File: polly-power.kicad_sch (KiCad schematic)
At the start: 53 parts, among them J1 Conn_02x04_Odd_Even, J2 Conn_02x05_Odd_Even, P1 Power, P2 Analog, P3 Digital, P4 Digital, P5 CONN_01X01, P6 CONN_01X01, P7 CONN_01X01, P8 CONN_01X01, P9 Arduino, Q1 BC547C, Q2 BC547C, U1 74LS04, U2 TL072, U3 74HC4051, U4 LM7805_TO220, U5 LM337_TO220, U6 MCP4922-EP, U7 MCP1541-TO, U8 LM4040LP-4.1

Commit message: Tidy up after migration
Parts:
- C10, C11, C4, C6, C9: symbol Device:CP1_Small -> Device:C_Polarized_Small
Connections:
- net -6.5V: now also C6.2; no longer C6.1
- net GNDA: now also C6.1; no longer C6.2
- no-connect marks 17 -> 18
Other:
- note added: "Voice param DAC multiplexer (pin 10/9/8): 1: CUTOFF 2: RESONANCE 3: MIXER 4: VCA 5: PWM 6: VCO_CV 7: WAVE_SEL 8: MOD_AMT"
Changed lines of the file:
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@@
   (junction (at 236.22 55.88) (diameter 0) (color 0 0 0 0)
   )
+  (junction (at 214.63 129.54) (diameter 0) (color 0 0 0 0)
+  )
   (junction (at 77.47 60.96) (diameter 0) (color 0 0 0 0)
   )
@@
   )
   (no_connect (at 125.73 121.92))
+  (no_connect (at 186.69 157.48))
   (no_connect (at 259.08 50.8))
   (no_connect (at 259.08 53.34))
@@
     (stroke (width 0) (type default) (color 0 0 0 0))
   )
+  (wire (pts (xy 215.9 127) (xy 214.63 127))
+    (stroke (width 0) (type default) (color 0 0 0 0))
+  )
   (wire (pts (xy 92.71 63.5) (xy 91.44 63.5))
     (stroke (width 0) (type default) (color 0 0 0 0))
@@
     (stroke (width 0) (type default) (color 0 0 0 0))
   )
+  (wire (pts (xy 214.63 127) (xy 214.63 129.54))
+    (stroke (width 0) (type default) (color 0 0 0 0))
+  )
   (wire (pts (xy 19.05 60.96) (xy 21.59 60.96))
     (stroke (width 0) (type default) (color 0 0 0 0))
@@
     (effects (font (size 1.27 1.27)) (justify left bottom))
   )
+  (text "Voice param DAC multiplexer (pin 10/9/8):\n\n1: CUTOFF\n2: RESONANCE\n3: MIXER\n4: VCA\n5: PWM\n6: VCO_CV\n7: WAVE_SEL\n8: MOD_AMT"
+    (at 298.45 54.61 0)
+    (effects (font (size 1.27 1.27)) (justify left bottom))
+  )
   (text "TL072" (at 82.55 30.48 0)
     (effects (font (size 1.27 1.27)) (justify left bottom))
@@
     (effects (font (size 1.27 1.27)) (justify right bottom))
   )
-  (label "~{LDAC}" (at 215.9 127 180)
-    (effects (font (size 1.27 1.27)) (justify right bottom))
-  )
   (label "2" (at 124.46 34.29 180)
     (effects (font (size 1.524 1.524)) (justify right bottom))
@@
     (effects (font (size 1.524 1.524)) (justify left bottom))
   )
-  (label "~{LDAC}" (at 48.26 25.4 0)
-    (effects (font (size 1.27 1.27)) (justify left bottom))
-  )
   (label "5V_DAC_REF" (at 44.45 60.96 0)
     (effects (font (size 1.27 1.27)) (justify left bottom))
@@
     (pin "1")
   )
-  (symbol (lib_id "Device:CP1_Small") (at 52.07 93.98 0) (unit 1)
+  (symbol (lib_id "Device:C_Polarized_Small") (at 52.07 93.98 0) (mirror x) (unit 1)
     (in_bom yes) (on_board yes)
-    (property "Reference" "C6" (id 0) (at 54.61 92.71 0)
+    (property "Reference" "C6" (id 0) (at 54.61 95.25 0)
       (effects (font (size 1.27 1.27)) (justify left))
     )
-    (property "Value" "10uF" (id 1) (at 54.61 95.25 0)
+    (property "Value" "10uF" (id 1) (at 54.61 92.71 0)
       (effects (font (size 1.27 1.27)) (justify left))
     )
@@
     (pin "1")
   )
-  (symbol (lib_id "Device:CP1_Small") (at 21.59 66.04 0) (unit 1)
+  (symbol (lib_id "Device:C_Polarized_Small") (at 21.59 66.04 0) (unit 1)
     (in_bom yes) (on_board yes)
     (property "Reference" "C4" (id 0) (at 19.05 64.77 0)
@@
     (pin "2")
   )
-  (symbol (lib_id "Device:CP1_Small") (at 39.37 160.02 0) (unit 1)
+  (symbol (lib_id "Device:C_Polarized_Small") (at 39.37 160.02 0) (unit 1)
     (in_bom yes) (on_board yes)
     (property "Reference" "C9" (id 0) (at 41.91 158.75 0)
@@
     (pin "1")
   )
-  (symbol (lib_id "Device:CP1_Small") (at 120.65 106.68 0) (unit 1)
+  (symbol (lib_id "Device:C_Polarized_Small") (at 120.65 106.68 0) (unit 1)
     (in_bom yes) (on_board yes)
     (property "Reference" "C10" (id 0) (at 123.19 105.41 0)
@@
     (pin "3")
   )
-  (symbol (lib_id "Device:CP1_Small") (at 142.24 121.92 90) (unit 1)
+  (symbol (lib_id "Device:C_Polarized_Small") (at 142.24 121.92 90) (unit 1)
     (in_bom yes) (on_board yes)
     (property "Reference" "C11" (id 0) (at 142.24 116.84 90))

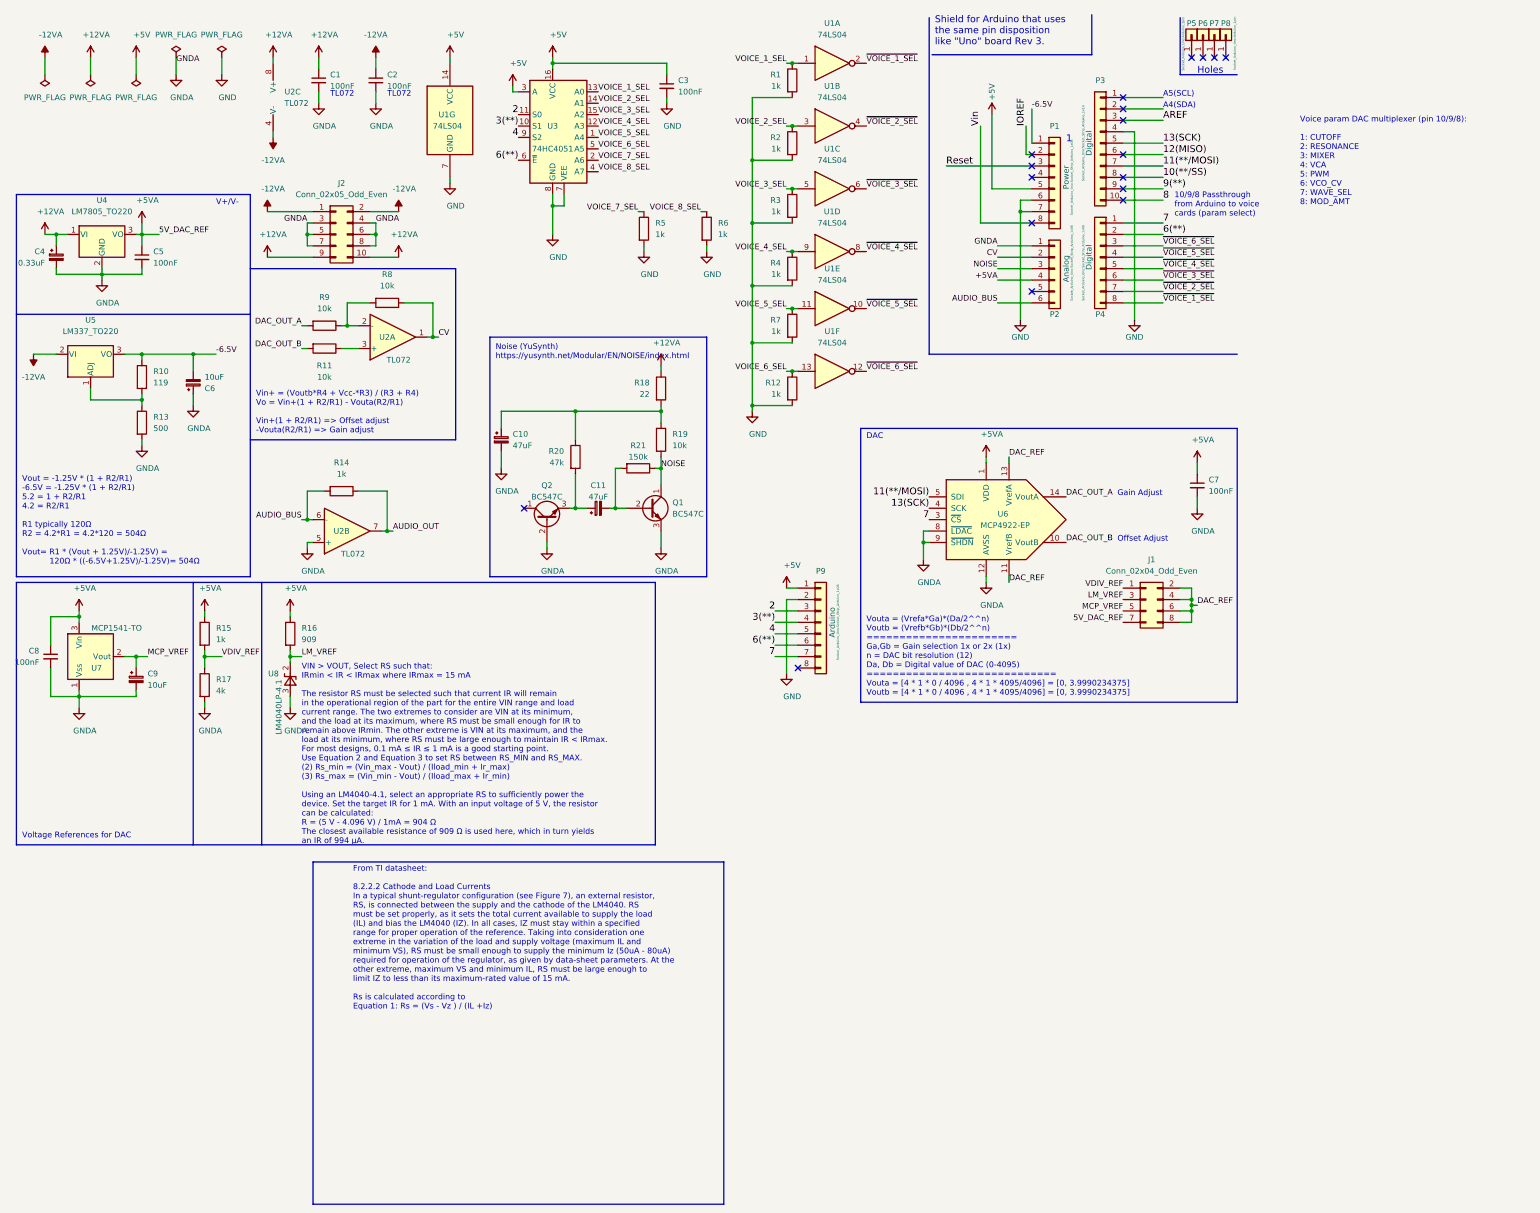
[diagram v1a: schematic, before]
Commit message: Split schematic into sheets
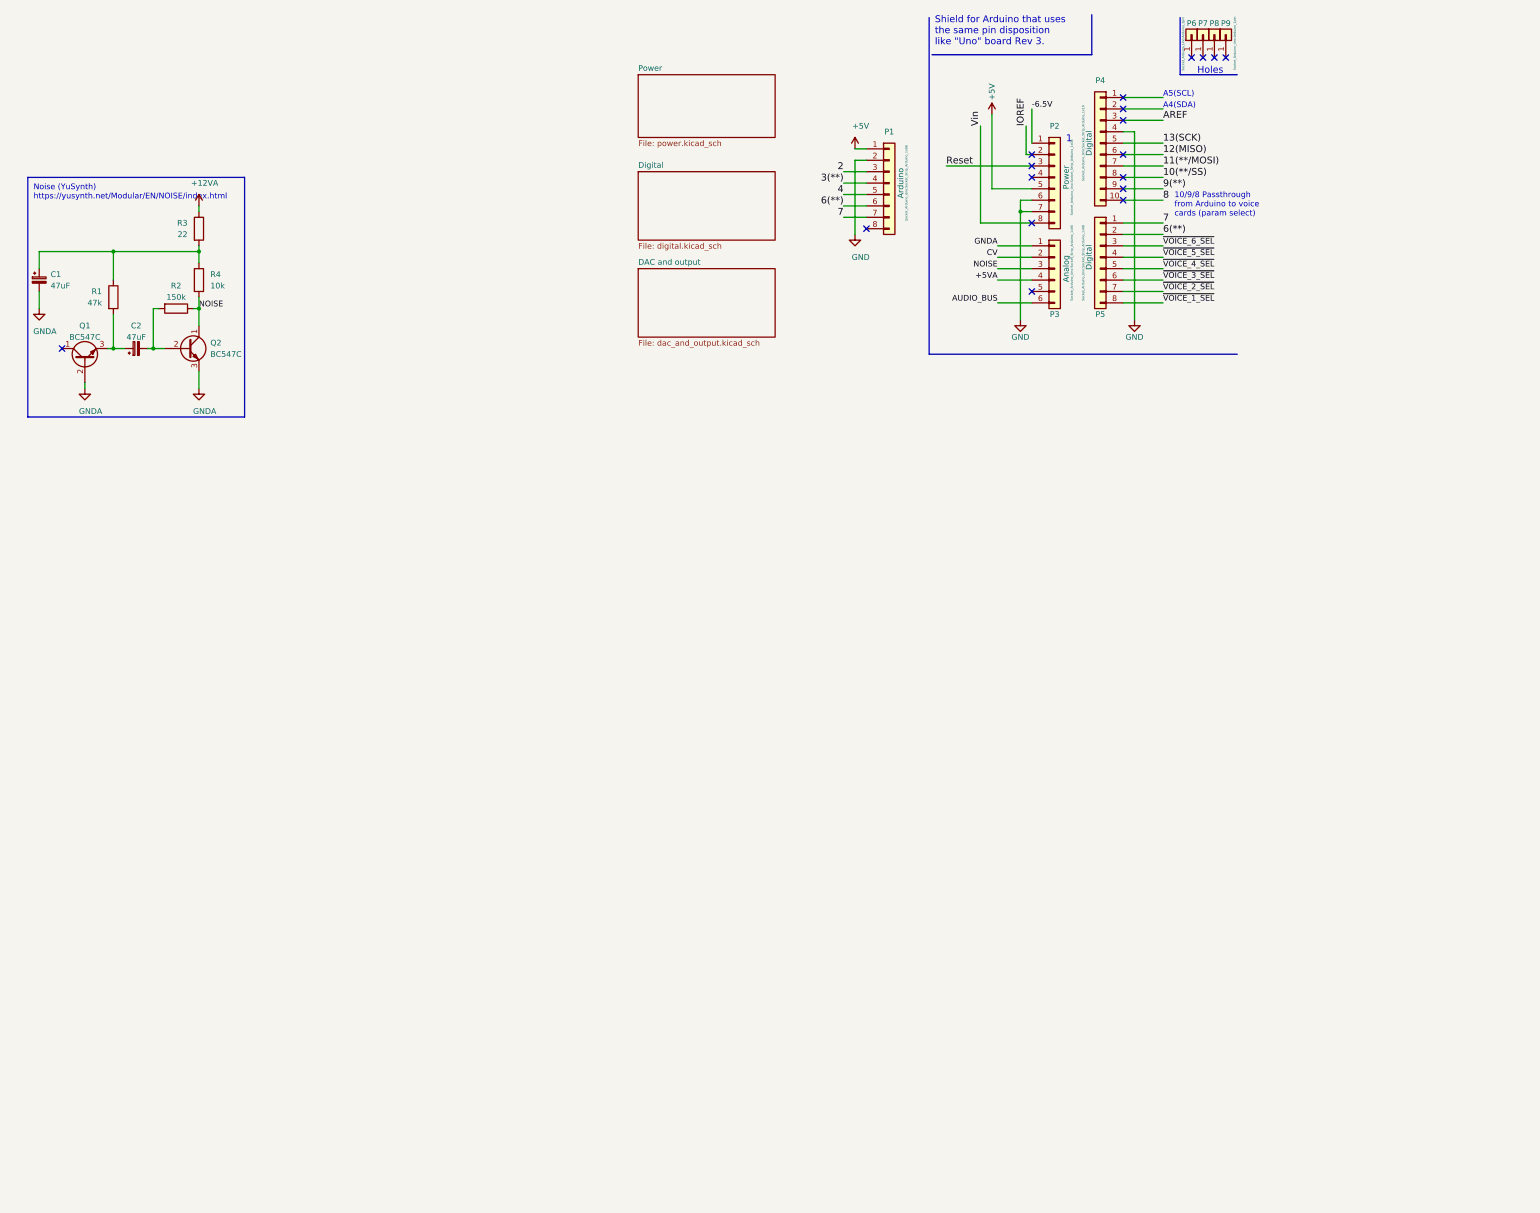
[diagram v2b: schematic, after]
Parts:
- removed C1, C2, C3, C5, C7, C8: 100nF, Capacitor_THT:C_Disc_D4.7mm_W2.5mm_P5.00mm, symbol Device:C_Small
- removed C4: 0.33uF, Capacitor_THT:CP_Radial_D6.3mm_P2.50mm, symbol Device:C_Polarized_Small
- removed C6, C9: 10uF, Capacitor_THT:CP_Radial_D6.3mm_P2.50mm, symbol Device:C_Polarized_Small
- removed J1: Conn_02x04_Odd_Even, Connector_PinHeader_2.54mm:PinHeader_2x04_P2.54mm_Vertical, symbol Connector_Generic:Conn_02x04_Odd_Even
- removed J2: Conn_02x05_Odd_Even, Connector_IDC:IDC-Header_2x05_P2.54mm_Vertical, symbol Connector_Generic:Conn_02x05_Odd_Even
- removed R1, R12, R14, R15, R2, R3, R4, R5, R6, R7: 1k, Resistor_THT:R_Axial_DIN0207_L6.3mm_D2.5mm_P7.62mm_Horizontal, symbol Device:R
- removed R10: 119, Resistor_THT:R_Axial_DIN0207_L6.3mm_D2.5mm_P7.62mm_Horizontal, symbol Device:R
- removed R11, R8, R9: 10k, Resistor_THT:R_Axial_DIN0207_L6.3mm_D2.5mm_P7.62mm_Horizontal, symbol Device:R
- removed R13: 500, Resistor_THT:R_Axial_DIN0207_L6.3mm_D2.5mm_P7.62mm_Horizontal, symbol Device:R
- removed R16: 909, Resistor_THT:R_Axial_DIN0207_L6.3mm_D2.5mm_P7.62mm_Horizontal, symbol Device:R
- removed R17: 4k, Resistor_THT:R_Axial_DIN0207_L6.3mm_D2.5mm_P7.62mm_Horizontal, symbol Device:R
- removed U1: 74LS04, Package_DIP:DIP-14_W7.62mm_Socket_LongPads, symbol 74xx:74LS04
- removed U2: TL072, Package_DIP:DIP-8_W7.62mm_Socket_LongPads, symbol Amplifier_Operational:TL072
- removed U3: 74HC4051, Package_DIP:DIP-16_W7.62mm_Socket_LongPads, symbol 74xx:74HC4051
- removed U4: LM7805_TO220, Package_TO_SOT_THT:TO-220-3_Vertical, symbol Regulator_Linear:LM7805_TO220
- removed U5: LM337_TO220, Package_TO_SOT_THT:TO-220-3_Vertical, symbol Regulator_Linear:LM337_TO220
- removed U6: MCP4922-EP, Package_DIP:DIP-14_W7.62mm_Socket_LongPads, symbol Analog_DAC:MCP4922-EP
- removed U7: MCP1541-TO, Package_TO_SOT_THT:TO-92_Inline_Wide, symbol Reference_Voltage:MCP1541-TO
- removed U8: LM4040LP-4.1, Package_TO_SOT_THT:TO-92_Inline_Wide, symbol Reference_Voltage:LM4040LP-4.1
- renumbered C10 to C1, C11 to C2, P9 to P1, P1 to P2, P2 to P3, P3 to P4, P4 to P5, P5 to P6, P6 to P7, P7 to P8, P8 to P9, Q2 to Q1, Q1 to Q2, R20 to R1, R21 to R2, R18 to R3, R19 to R4
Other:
- added sheet DAC and output (dac_and_output.kicad_sch)
- added sheet Digital (digital.kicad_sch)
- added sheet Power (power.kicad_sch)
- note removed: "DAC"
- note removed: "From TI datasheet: 8.2.2.2 Cathode and Load Currents In a typical shunt-regulator configuration (see Figure 7), an external resistor, RS, is connected between the supply and the cathode of the LM4040. RS must be set properly, as it sets the total current available to supply the load (IL) and bias the LM4040 (IZ). In all cases, IZ must stay within a specified range for proper operation of the refe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"
- note removed: "Gain Adjust"
- note removed: "Offset Adjust"
- note removed: "TL072"
- note removed: "V+/V-"
- note removed: "VIN > VOUT, Select RS such that: IRmin < IR < IRmax where IRmax = 15 mA The resistor RS must be selected such that current IR will remain in the operational region of the part for the entire VIN range and load current range. The two extremes to consider are VIN at its minimum, and the load at its maximum, where RS must be small enough for IR to remain above IRmin. The other extreme is VIN at its 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"
- note removed: "Vin+ = (Voutb*R4 + Vcc-*R3) / (R3 + R4) Vo = Vin+(1 + R2/R1) - Vouta(R2/R1) Vin+(1 + R2/R1) => Offset adjust -Vouta(R2/R1) => Gain adjust"
- note removed: "Voice param DAC multiplexer (pin 10/9/8): 1: CUTOFF 2: RESONANCE 3: MIXER 4: VCA 5: PWM 6: VCO_CV 7: WAVE_SEL 8: MOD_AMT"
- note removed: "Voltage References for DAC"
- note removed: "Vout = -1.25V * (1 + R2/R1) -6.5V = -1.25V * (1 + R2/R1) 5.2 = 1 + R2/R1 4.2 = R2/R1 R1 typically 120Ω R2 = 4.2*R1 = 4.2*120 = 504Ω Vout= R1 * (Vout + 1.25V)/-1.25V) = 120Ω * ((-6.5V+1.25V)/-1.25V)= 504Ω"
- note removed: "Vouta = (Vrefa*Ga)*(Da/2^^n) Voutb = (Vrefb*Gb)*(Db/2^^n) ======================= Ga,Gb = Gain selection 1x or 2x (1x) n = DAC bit resolution (12) Da, Db = Digital value of DAC (0-4095) ============================= Vouta = [4 * 1 * 0 / 4096 , 4 * 1 * 4095/4096] = [0, 3.9990234375] Voutb = [4 * 1 * 0 / 4096 , 4 * 1 * 4095/4096] = [0, 3.9990234375]"
- moved on the sheet: C1, C2, P1, Q1, Q2, R1, R2, R3, R4
